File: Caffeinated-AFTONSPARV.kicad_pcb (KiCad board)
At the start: 2 copper layers, 42.5 x 16.1 mm, 3 parts, among them J1 Conn_01x02, J2 Conn_01x04, SW1 SW_Push

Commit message: feat(): Finalize design
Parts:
- added C1: 100nF, Capacitor_SMD:C_0603_1608Metric, F.Cu at (163.0, 93.5)
- added C2: 100µF 35V, Capacitor_THT:CP_Radial_D6.3mm_P2.50mm, B.Cu at (161.8, 95.3)
- added C3: 4.7uF, Capacitor_SMD:C_0805_2012Metric, B.Cu at (170.9, 100.0)
- added C4: 100nF, Capacitor_SMD:C_0603_1608Metric, F.Cu at (168.7, 99.4)
- added C5: 22uF, Capacitor_SMD:C_0603_1608Metric, B.Cu at (169.2, 105.0)
- added C6: 22uF, Capacitor_SMD:C_0603_1608Metric, F.Cu at (169.3, 105.0)
- added G***: LOGO, LOGO, F.Cu at (135.3, 104.0)
- added J3: TagConnect, Connector:Tag-Connect_TC2030-IDC-NL_2x03_P1.27mm_Vertical, F.Cu at (151.8, 104.7)
- added L1: 10uH, PCM_Inductor_SMD_AKL:L_1206_3216Metric, B.Cu at (168.5, 101.0)
- added Q1: AO3400A, Package_TO_SOT_SMD:SOT-23, B.Cu at (163.9, 101.0)
- added Q2: AO3400A, Package_TO_SOT_SMD:SOT-23, B.Cu at (160.4, 101.0)
- added Q3: AO3400A, Package_TO_SOT_SMD:SOT-23, B.Cu at (156.9, 101.0)
- added R1: 10k, Resistor_SMD:R_0603_1608Metric, B.Cu at (156.0, 104.4)
- added R10: 10k, Resistor_SMD:R_0603_1608Metric, F.Cu at (142.8, 100.4)
- added R11: 1, Resistor_SMD:R_0603_1608Metric, B.Cu at (170.9, 95.9)
- added R12: 10k, Resistor_SMD:R_0603_1608Metric, B.Cu at (167.7, 105.0)
- added R13: 18k, Resistor_SMD:R_0603_1608Metric, F.Cu at (167.8, 105.0)
- added R14: 10k, Resistor_SMD:R_0603_1608Metric, F.Cu at (171.1, 102.0)
- added R2: 10k, Resistor_SMD:R_0603_1608Metric, B.Cu at (159.5, 104.4)
- added R3: 10k, Resistor_SMD:R_0603_1608Metric, B.Cu at (163.0, 104.4)
- added R4: 470, Resistor_SMD:R_0603_1608Metric, B.Cu at (161.3, 104.4)
- added R5: 470, Resistor_SMD:R_0603_1608Metric, B.Cu at (157.8, 104.4)
- added R6: 470, Resistor_SMD:R_0603_1608Metric, B.Cu at (164.8, 104.4)
- added R7: 10k, Resistor_SMD:R_0603_1608Metric, F.Cu at (163.4, 104.6)
- added R8: 10k, Resistor_SMD:R_0603_1608Metric, F.Cu at (141.3, 100.4)
- added R9: 10k, Resistor_SMD:R_0603_1608Metric, F.Cu at (144.3, 100.4)
- added REF**: OSHW-Logo2_7.3x6mm_SilkScreen, Symbol:OSHW-Logo2_7.3x6mm_SilkScreen, F.Cu at (135.3, 96.0)
- added U1: ESP32-C3-MINI-1, PCM_Espressif:ESP32-C3-MINI-1, B.Cu at (139.6, 100.0)
- added U2: SY8201ABC, Package_TO_SOT_SMD:SOT-23-6, F.Cu at (168.3, 101.8)
- moved J1 36.1 mm to (168.3, 96.4)
- moved J2 16.7 mm to (150.2, 94.1)
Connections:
- SW1 pad 1: unconnected-(SW1-Pad1) -> GND
- SW1 pad 2: unconnected-(SW1-Pad2) -> Net-(J3-IO0/IO8)
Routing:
- net GND: track 0.00 -> 81.5 mm, vias 0 -> 18
- net +3.3V: track 0.00 -> 67.2 mm, vias 0 -> 3
- net Net-(J3-IO0/IO8): track 0.00 -> 30.3 mm, vias 0 -> 2
- net Net-(J3-EN): track 0.00 -> 22.4 mm, vias 0 -> 3
- net Net-(U1-GPIO6): track 0.00 -> 22.1 mm
- net +24V: track 0.00 -> 18.4 mm
- net Net-(U1-GPIO5/ADC2_CH0): track 0.00 -> 18.2 mm
- net Net-(J3-TX): track 0.00 -> 14.3 mm, vias 0 -> 3
- net Net-(U1-GPIO4/ADC1_CH4): track 0.00 -> 14.3 mm
- net Net-(J2-Pin_3): track 0.00 -> 13.1 mm
- net Net-(J2-Pin_2): track 0.00 -> 12.5 mm
- net Net-(J3-RX): track 0.00 -> 12.2 mm, vias 0 -> 1
- net Net-(J2-Pin_1): track 0.00 -> 11.9 mm
- net Net-(U2-IN): track 0.00 -> 8.09 mm, vias 0 -> 1
- net Net-(U2-FB): track 0.00 -> 7.28 mm, vias 0 -> 1
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- added copper zone on B.Cu, net +3.3V
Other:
- board text added: "Caffeinated AFTONSPARV"
- board text added: "OSHWID: 0000"
- board text added: "caffeinated-labs.org"
- board text added: "v0.1"

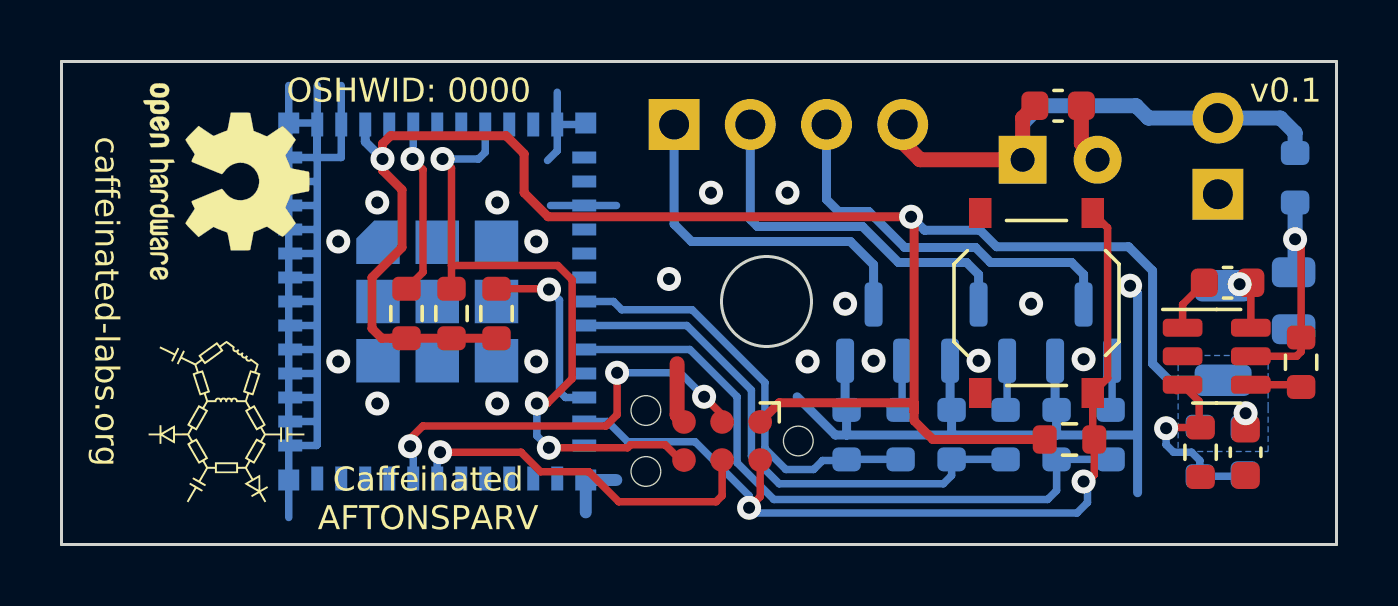
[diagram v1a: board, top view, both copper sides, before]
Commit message: feat(): Rework pcb to 4 layers
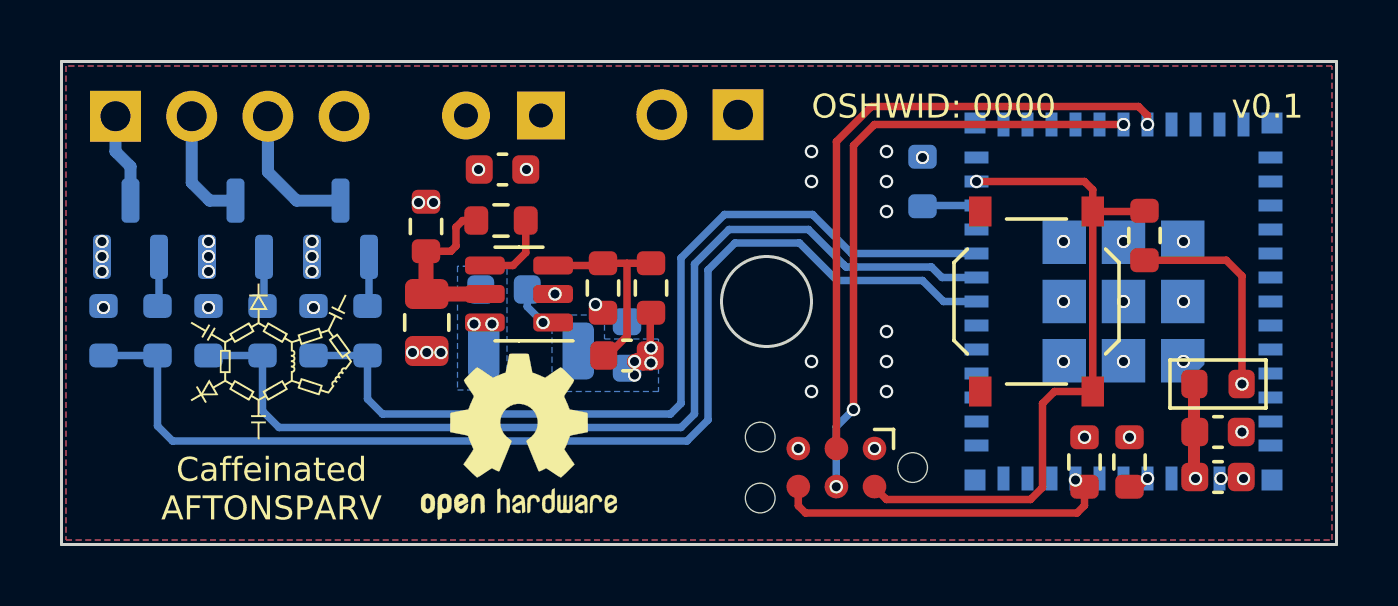
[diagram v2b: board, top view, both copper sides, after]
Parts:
- added C7: 100nF, Capacitor_SMD:C_0603_1608Metric, F.Cu at (168.3, 104.3)
- added C8: 100uF, Capacitor_SMD:C_0603_1608Metric, F.Cu at (168.3, 105.8)
- added FB1: FerriteBead, PCM_Ferrite_SMD_AKL:Ferrite_0603_1608Metric, F.Cu at (168.3, 102.8)
- C3, R11: moved to F.Cu
- C4, C6, R9: moved to B.Cu
- C5: value 22uF -> 22pF; moved to F.Cu
- R12: value 10k -> 100k; moved to F.Cu
- R13: value 18k -> 22,1k
- moved R11 29.0 mm to (141.9, 97.5)
- moved C3 28.9 mm to (142.0, 100.7)
- moved U1 28.3 mm to (167.9, 100.0), turned to 90 degrees
- moved R14 27.1 mm to (144.4, 97.3), turned to 0 degrees
- moved Q1 25.0 mm to (139.1, 97.6)
- moved Q2 25.0 mm to (135.6, 97.6)
- moved Q3 25.0 mm to (132.1, 97.6)
- moved R1 25.0 mm to (131.2, 101.0)
- moved R2 25.0 mm to (134.7, 101.0)
- moved R3 25.0 mm to (138.2, 101.0)
- moved R4 25.0 mm to (136.5, 101.0)
- moved R5 25.0 mm to (133.0, 101.0)
- moved R6 25.0 mm to (140.0, 101.0)
- moved R8 24.6 mm to (165.4, 105.3), turned to -90 degrees
- moved C4 24.1 mm to (144.6, 99.6), turned to 0 degrees
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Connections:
- U1 pad 3: +3.3V -> Net-(U1-3V3)
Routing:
- net GND: track 81.5 -> 0.00 mm, vias 18 -> 41
- net +3.3V: track 67.2 -> 10.4 mm, vias 3 -> 9
- net Net-(U1-GPIO4/ADC1_CH4): track 14.3 -> 38.1 mm
- net +24V: track 18.4 -> 0.00 mm, vias 0 -> 3
- net Net-(U1-GPIO5/ADC2_CH0): track 18.2 -> 34.0 mm
- net Net-(J3-EN): track 22.4 -> 11.0 mm, vias 3 -> 1
- net Net-(J3-RX): track 12.2 -> 21.2 mm, vias 1 -> 3
- net Net-(J2-Pin_1): track 11.9 -> 3.02 mm
- net Net-(J2-Pin_2): track 12.5 -> 3.92 mm
- net Net-(J2-Pin_3): track 13.1 -> 4.67 mm
- net Net-(U1-GPIO6): track 22.1 -> 29.9 mm
- net Net-(J3-IO0/IO8): track 30.3 -> 23.1 mm, vias 2 -> 1
- net Net-(J3-TX): track 14.3 -> 21.5 mm, vias 3 -> 1
- net Net-(U1-GPIO2/ADC1_CH2): track 5.86 -> 0.71 mm
- net Net-(U1-GPIO8): track 6.21 -> 1.93 mm, vias 1 -> 0
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- added copper zone on In2.Cu, net +24V
- added copper zone on In2.Cu, net +3.3V
- added copper zone on In1.Cu, net GND
- added copper zone on B.Cu, net Net-(U2-LX)
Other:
- copper layers 2 -> 4
- board text added: "caffeinated-labs.org/aftonsparv"
- board text removed: "caffeinated-labs.org"

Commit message: feat(): Rework and finalize design
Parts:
- removed C8: 100uF, Capacitor_SMD:C_0603_1608Metric
- removed FB1: FerriteBead, PCM_Ferrite_SMD_AKL:Ferrite_0603_1608Metric
- added C10: 4.7uF, Capacitor_SMD:C_0805_2012Metric, B.Cu at (140.1, 104.2)
- added C11: 100nF, Capacitor_SMD:C_0603_1608Metric, B.Cu at (140.3, 105.9)
- added C9: 4.7uF, Capacitor_SMD:C_0805_2012Metric, B.Cu at (140.1, 102.2)
- added J4: USB, Connector_PinSocket_1.00mm:PinSocket_1x04_P1.00mm_Vertical, F.Cu at (155.4, 93.0)
- C1, C3, C5, C7, U2: moved to B.Cu
- C6: value 22uF -> 4.7uF; footprint Capacitor_SMD:C_0603_1608Metric -> Capacitor_SMD:C_0805_2012Metric
- J1: value Conn_01x02 -> PWR
- J2: value Conn_01x04 -> LED
- R1, R2, R3, R9: value 10k -> 10kΩ
- R10, R14, R7, R8: value 10k -> 10kΩ; moved to B.Cu
- R11: value 1 -> 1Ω; moved to B.Cu
- R12: value 100k -> 100kΩ; moved to B.Cu
- R13: value 22,1k -> 22.1kΩ; moved to B.Cu
- R4, R5, R6: value 470 -> 20Ω
- SW1: footprint Button_Switch_SMD:SW_Push_1P1T_XKB_TS-1187A -> caffeinated-labs:YTS-C005
- U1: value ESP32-C3-MINI-1 -> ESP32-C3-MINI-1-[H/N]4
- moved R7 17.7 mm to (149.8, 105.2)
- moved R10 12.6 mm to (151.3, 105.2), turned to 90 degrees
- moved R8 12.6 mm to (157.0, 96.0)
- moved C7 11.9 mm to (156.7, 102.0), turned to 90 degrees
- moved C6 9.76 mm to (158.4, 101.8), turned to 90 degrees
- moved R12 9.37 mm to (140.2, 98.2)
- moved Q1 9.25 mm to (132.7, 104.2), turned to 180 degrees
- moved C5 7.79 mm to (141.0, 100.5), turned to 180 degrees
- moved R11 7.61 mm to (149.3, 99.5)
- moved C1 6.74 mm to (151.2, 96.3), turned to 0 degrees
- moved REF** 6.72 mm to (144.5, 97.8)
- moved R13 6.22 mm to (141.8, 98.2)
- moved C3 6.13 mm to (147.7, 103.0)
- moved R1 5.63 mm to (136.1, 98.2), turned to 180 degrees
- moved R5 5.53 mm to (136.1, 96.4), turned to 180 degrees
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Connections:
- net Net-(J3-EN) renamed EN
- net Net-(J3-IO0/IO8) renamed IO9
- net Net-(J3-RX) renamed RX
- net Net-(J3-TX) renamed TX
- net Net-(U1-GPIO5/ADC2_CH0) renamed LED-G
- C6 pad 1: GND -> +3.3V
- C6 pad 2: +3.3V -> GND
- C7 pad 1: Net-(U1-3V3) -> +3.3V
- R1 pad 1: Net-(U1-GPIO4/ADC1_CH4) -> LED-B
- R3 pad 1: Net-(U1-GPIO6) -> LED-R
- R5 pad 1: Net-(U1-GPIO4/ADC1_CH4) -> LED-B
- R6 pad 1: Net-(U1-GPIO6) -> LED-R
- U1 pad 18: Net-(U1-GPIO4/ADC1_CH4) -> LED-R
- U1 pad 20: Net-(U1-GPIO6) -> LED-B
- U1 pad 26: unconnected-(U1-GPIO18/USB_D--Pad26) -> USB-D-
- U1 pad 27: unconnected-(U1-GPIO19/USB_D+-Pad27) -> USB-D+
- U1 pad 3: Net-(U1-3V3) -> +3.3V
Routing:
- net Net-(U1-GPIO4/ADC1_CH4): track 38.1 -> 0.00 mm
- net LED-R: track 0.00 -> 31.8 mm, vias 0 -> 2
- net Net-(U1-GPIO6): track 29.9 -> 0.00 mm
- net LED-B: track 0.00 -> 26.0 mm, vias 0 -> 2
- net Net-(U1-GPIO2/ADC1_CH2): track 0.71 -> 17.0 mm, vias 1 -> 2
- net Net-(J2-Pin_3): track 4.67 -> 15.4 mm, vias 0 -> 2
- net Net-(J2-Pin_2): track 3.92 -> 12.5 mm, vias 0 -> 2
- net IO9: track 23.1 -> 31.3 mm, vias 1 -> 2
- net USB-D+: track 0.00 -> 7.80 mm, vias 0 -> 1
- net USB-D-: track 0.00 -> 5.39 mm, vias 0 -> 1
- net LED-G: track 34.0 -> 29.0 mm, vias 0 -> 2
- net +3.3V: track 10.4 -> 15.1 mm
- net EN: track 11.0 -> 15.2 mm, vias 1 -> 2
- net Net-(U1-3V3): track 3.19 -> 0.00 mm, vias 1 -> 0
- net Net-(U2-BS): track 1.32 -> 4.50 mm, vias 1 -> 0
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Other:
- board text added: "3V3"
- board text added: "EN"
- board text added: "GND"
- board text added: "IO8"
- board text added: "OSHWID: DE000140"
- board text added: "RX"
- board text added: "TX"
- board text added: "USB+"
- board text added: "USB-"
- board text removed: "OSHWID: 0000"

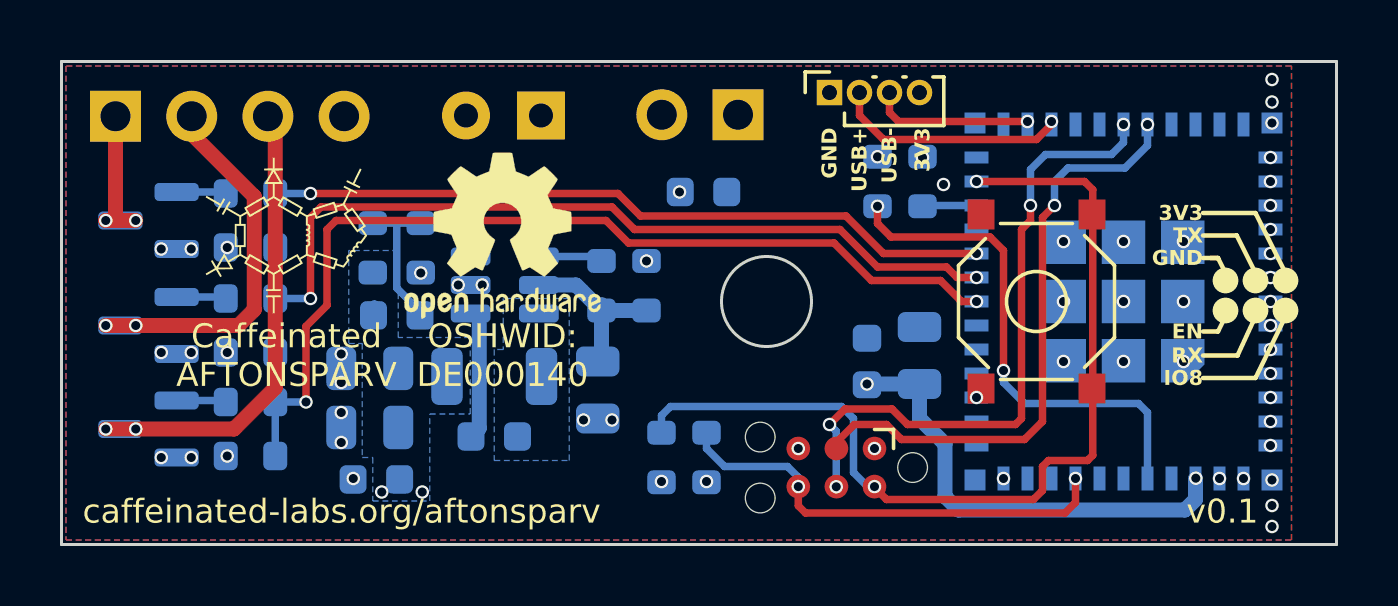
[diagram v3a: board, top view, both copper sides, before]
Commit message: feat(): Replace L1 footprint and add Refs
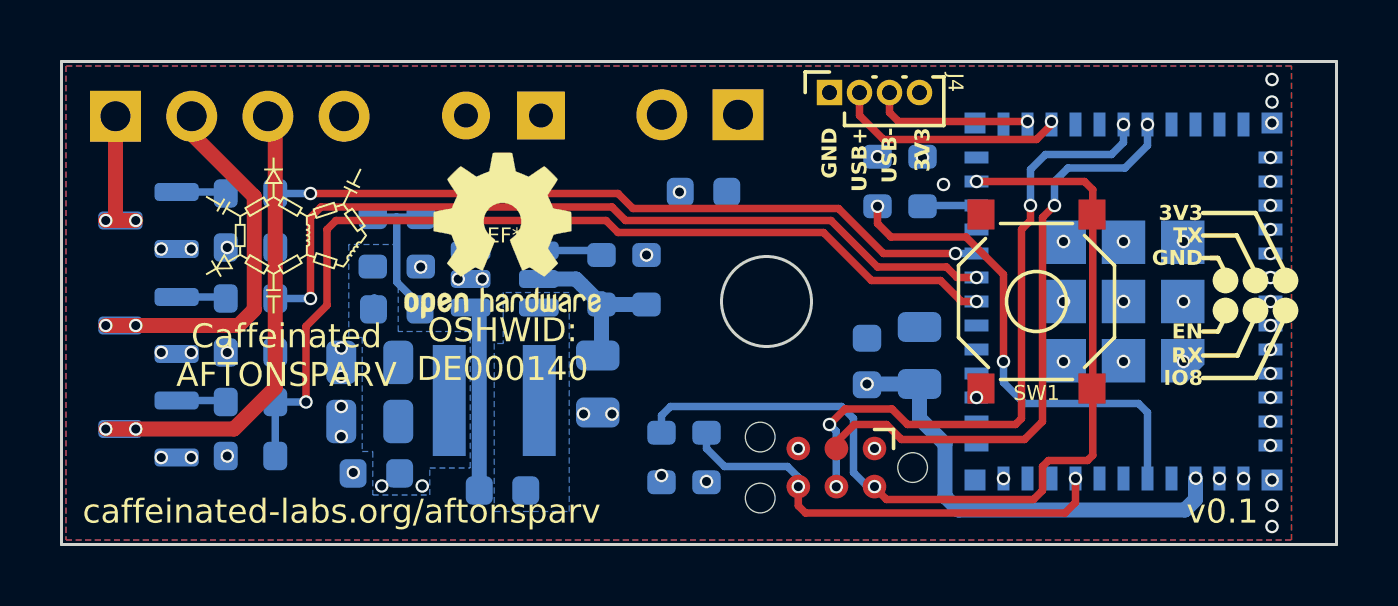
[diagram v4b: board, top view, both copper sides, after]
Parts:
- L1: footprint PCM_Inductor_SMD_AKL:L_1206_3216Metric -> Inductor_SMD:L_Sunlord_SWPA4030S
- moved C4 1.82 mm to (144.5, 106.3)
- moved L1 0.80 mm to (144.2, 103.3)
- moved C10 0.20 mm to (140.1, 104.0)
- moved C11 0.20 mm to (140.3, 105.7)
- moved C3 0.20 mm to (147.7, 102.8)
- moved C5 0.20 mm to (141.0, 100.3)
- moved C9 0.20 mm to (140.1, 102.0)
- moved R12 0.20 mm to (140.2, 98.0)
- moved R13 0.20 mm to (141.8, 98.0)
- moved U2 0.20 mm to (144.6, 99.2)
- moved R11 0.20 mm to (149.3, 99.3)
- moved R14 0.20 mm to (147.8, 99.3)
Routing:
- net Net-(U2-BS): track 4.50 -> 6.39 mm

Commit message: refactor(): Move vias
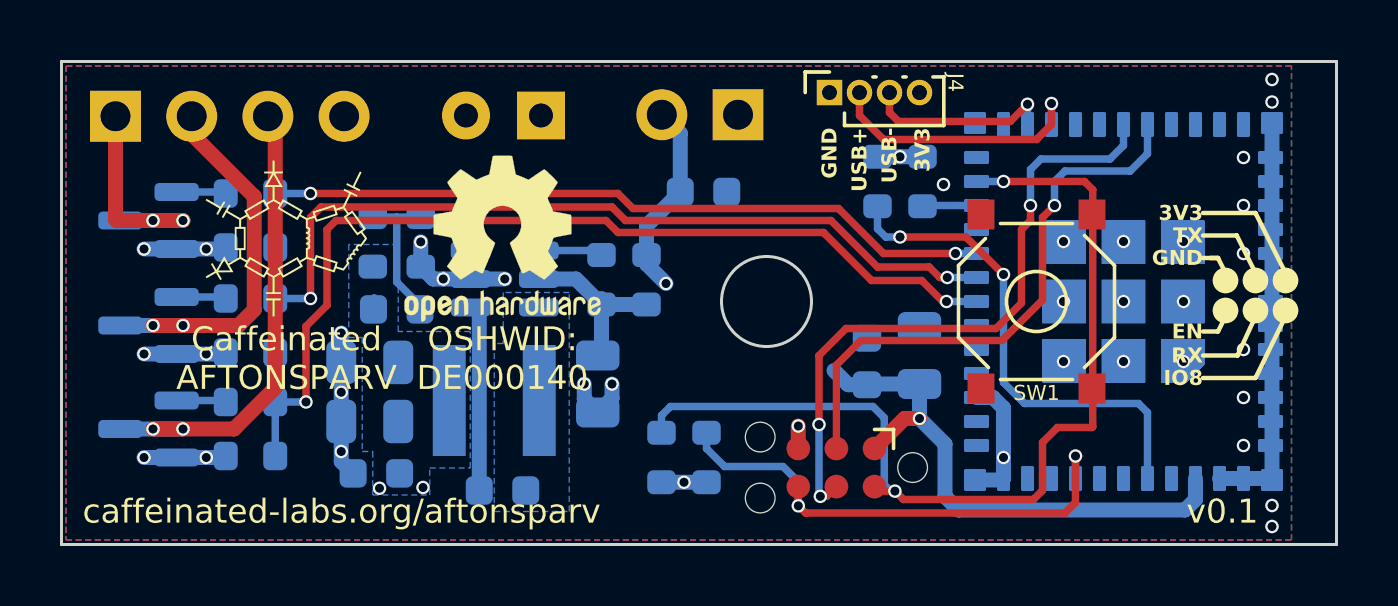
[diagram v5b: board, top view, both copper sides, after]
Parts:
- added U1: ESP32-C3-MINI-1-[H/N]4, PCM_Espressif:ESP32-C3-MINI-1, B.Cu at (167.9, 100.0)
- moved G*** 0.10 mm to (137.3, 97.9)
- moved REF** 0.10 mm to (144.5, 97.9)
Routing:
- net GND: track 0.00 -> 37.9 mm, vias 53 -> 36
- net +24V: track 0.00 -> 6.61 mm, vias 2 -> 1
- net +3.3V: track 15.1 -> 21.3 mm, vias 9 -> 5
- net Net-(J2-Pin_1): track 4.77 -> 7.78 mm
- net EN: track 15.2 -> 17.3 mm
- net USB-D+: track 7.80 -> 9.10 mm
- net TX: track 20.2 -> 19.1 mm, vias 2 -> 1
- net USB-D-: track 5.39 -> 6.30 mm
- net IO9: track 31.3 -> 32.2 mm
- net Net-(J2-Pin_3): track 15.4 -> 15.9 mm
- net Net-(J2-Pin_2): track 12.5 -> 13.0 mm
- net RX: vias 4 -> 3

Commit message: feat(pcb): Set drill pos and export settings
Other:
- board text added: "JLCJLCJLCJLC"
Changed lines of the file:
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@@
     (pad_to_mask_clearance 0)
     (aux_axis_origin 129.8 108.1)
-    (grid_origin 132.85 97.3)
+    (grid_origin 153.3 100)
     (pcbplotparams
       (layerselection 0x00010fc_ffffffff)
@@
       (outputformat 1)
       (mirror false)
-      (drillshape 1)
+      (drillshape 0)
       (scaleselection 1)
-      (outputdirectory "")
+      (outputdirectory "GERBER")
     )
   )
@@
   (gr_rect locked (start 171.3 106.1) (end 172.3 108.1)
     (stroke (width 0.05) (type default)) (fill none) (layer "B.CrtYd"))
+  (gr_text "JLCJLCJLCJLC" (at 168.5 99.9 90) (layer "B.SilkS")
+    (effects (font (size 0.8 0.8) (thickness 0.15) bold) (justify mirror))
+  )
   (gr_text "USB-" (at 157.4 94.2 90) (layer "F.SilkS")
     (effects (font (size 0.5 0.5) (thickness 0.1) bold) (justify right))
